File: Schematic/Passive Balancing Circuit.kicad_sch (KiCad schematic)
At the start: 70 parts, among them Q1 DMN2004K, Q2 DMN2004K, Q3 DMN2004K, Q4 DMN2004K, Q5 DMN2004K, Q6 DMN2004K, Q7 DMN2004K, Q8 DMN2004K

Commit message: 1st Schematic Review
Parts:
- renumbered C7 to C10, C8 to C11, C9 to C12, C10 to C13, C1 to C4, C2 to C5, C3 to C6, C4 to C7, C5 to C8, C6 to C9, R8 to R10, R9 to R11, R10 to R12, R11 to R13, R12 to R14, R13 to R15, R14 to R16, R15 to R17, R16 to R18, R17 to R19, R18 to R20, R19 to R21, R20 to R22, R21 to R23, R22 to R24, R23 to R25, R24 to R26, R25 to R27, R26 to R28, R27 to R29, R1 to R3, R28 to R30, R29 to R31, R30 to R32, R31 to R33, R32 to R34, R33 to R35, R34 to R36, R35 to R37, R2 to R4, R3 to R5, R4 to R6, R5 to R7, R6 to R8, R7 to R9

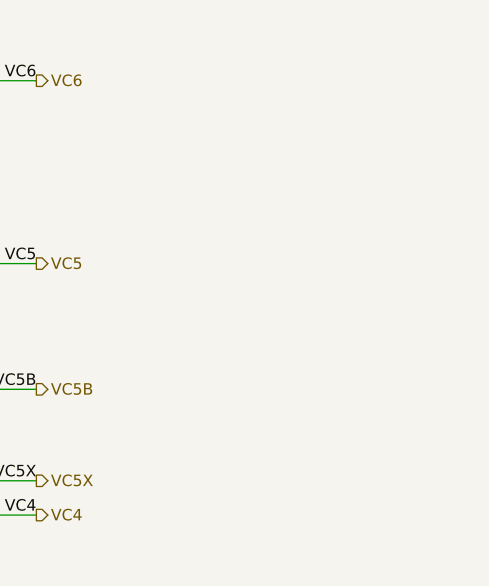
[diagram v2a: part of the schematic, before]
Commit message: added so many test points
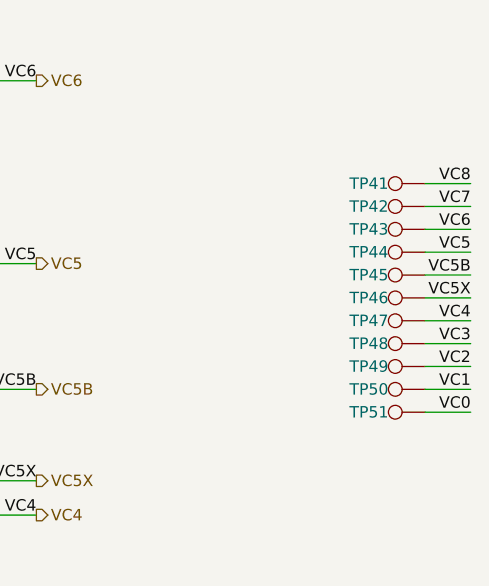
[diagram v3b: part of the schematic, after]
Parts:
- added TP41, TP42, TP43, TP44, TP45, TP46, TP47, TP48, TP49, TP50, TP51: TestPoint, symbol Connector:TestPoint
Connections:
- net VC0: now also TP51.1
- net VC1: now also TP50.1
- net VC2: now also TP49.1
- net VC3: now also TP48.1
- net VC4: now also TP47.1
- net VC5: now also TP44.1
- net VC5B: now also TP45.1
- net VC5X: now also TP46.1
- net VC6: now also TP43.1
- net VC7: now also TP42.1
- net VC8: now also TP41.1

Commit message: updates
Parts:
- renumbered TP41 to TP40, TP42 to TP41, TP43 to TP42, TP44 to TP43, TP45 to TP44, TP46 to TP45, TP47 to TP46, TP48 to TP47, TP49 to TP48, TP50 to TP49, TP51 to TP50
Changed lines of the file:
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@@
 		(on_board yes)
 		(dnp no)
-		(property "Reference" "TP41"
+		(property "Reference" "TP40"
 			(at 195.326 68.58 90)
 			(effects
@@
 			(project "STAR"
 				(path "/fc8533bc-25dd-4c20-9b4c-ffebebd6739b/e8da5d81-614b-4fe5-84b3-4c351fab7114/2e07670d-30e4-461b-a69e-227505cf7e3a"
-					(reference "TP41")
+					(reference "TP40")
 					(unit 1)
 				)
@@
 		(on_board yes)
 		(dnp no)
-		(property "Reference" "TP48"
+		(property "Reference" "TP47"
 			(at 195.326 86.36 90)
 			(effects
@@
 			(project "STAR"
 				(path "/fc8533bc-25dd-4c20-9b4c-ffebebd6739b/e8da5d81-614b-4fe5-84b3-4c351fab7114/2e07670d-30e4-461b-a69e-227505cf7e3a"
-					(reference "TP48")
+					(reference "TP47")
 					(unit 1)
 				)
@@
 		(on_board yes)
 		(dnp no)
-		(property "Reference" "TP49"
+		(property "Reference" "TP48"
 			(at 195.326 88.9 90)
 			(effects
@@
 			(project "STAR"
 				(path "/fc8533bc-25dd-4c20-9b4c-ffebebd6739b/e8da5d81-614b-4fe5-84b3-4c351fab7114/2e07670d-30e4-461b-a69e-227505cf7e3a"
-					(reference "TP49")
+					(reference "TP48")
 					(unit 1)
 				)
@@
 		(on_board yes)
 		(dnp no)
-		(property "Reference" "TP44"
+		(property "Reference" "TP43"
 			(at 195.326 76.2 90)
 			(effects
@@
 			(project "STAR"
 				(path "/fc8533bc-25dd-4c20-9b4c-ffebebd6739b/e8da5d81-614b-4fe5-84b3-4c351fab7114/2e07670d-30e4-461b-a69e-227505cf7e3a"
-					(reference "TP44")
+					(reference "TP43")
 					(unit 1)
 				)
@@
 		(on_board yes)
 		(dnp no)
-		(property "Reference" "TP47"
+		(property "Reference" "TP46"
 			(at 195.326 83.82 90)
 			(effects
@@
 			(project "STAR"
 				(path "/fc8533bc-25dd-4c20-9b4c-ffebebd6739b/e8da5d81-614b-4fe5-84b3-4c351fab7114/2e07670d-30e4-461b-a69e-227505cf7e3a"
-					(reference "TP47")
+					(reference "TP46")
 					(unit 1)
 				)
@@
 		(on_board yes)
 		(dnp no)
-		(property "Reference" "TP43"
+		(property "Reference" "TP42"
 			(at 195.326 73.66 90)
 			(effects
@@
 			(project "STAR"
 				(path "/fc8533bc-25dd-4c20-9b4c-ffebebd6739b/e8da5d81-614b-4fe5-84b3-4c351fab7114/2e07670d-30e4-461b-a69e-227505cf7e3a"
-					(reference "TP43")
+					(reference "TP42")
 					(unit 1)
 				)
@@
 		(on_board yes)
 		(dnp no)
-		(property "Reference" "TP45"
+		(property "Reference" "TP44"
 			(at 195.326 78.74 90)
 			(effects
@@
 			(project "STAR"
 				(path "/fc8533bc-25dd-4c20-9b4c-ffebebd6739b/e8da5d81-614b-4fe5-84b3-4c351fab7114/2e07670d-30e4-461b-a69e-227505cf7e3a"
-					(reference "TP45")
+					(reference "TP44")
 					(unit 1)
 				)
@@
 		(on_board yes)
 		(dnp no)
-		(property "Reference" "TP46"
+		(property "Reference" "TP45"
 			(at 195.326 81.28 90)
 			(effects
@@
 			(project "STAR"
 				(path "/fc8533bc-25dd-4c20-9b4c-ffebebd6739b/e8da5d81-614b-4fe5-84b3-4c351fab7114/2e07670d-30e4-461b-a69e-227505cf7e3a"
-					(reference "TP46")
+					(reference "TP45")
 					(unit 1)
 				)
@@
 		(on_board yes)
 		(dnp no)
-		(property "Reference" "TP51"
+		(property "Reference" "TP50"
 			(at 195.326 93.98 90)
 			(effects
@@
 			(project "STAR"
 				(path "/fc8533bc-25dd-4c20-9b4c-ffebebd6739b/e8da5d81-614b-4fe5-84b3-4c351fab7114/2e07670d-30e4-461b-a69e-227505cf7e3a"
-					(reference "TP51")
+					(reference "TP50")
 					(unit 1)
 				)
@@
 		(on_board yes)
 		(dnp no)
-		(property "Reference" "TP50"
+		(property "Reference" "TP49"
 			(at 195.326 91.44 90)
 			(effects
@@
 			(project "STAR"
 				(path "/fc8533bc-25dd-4c20-9b4c-ffebebd6739b/e8da5d81-614b-4fe5-84b3-4c351fab7114/2e07670d-30e4-461b-a69e-227505cf7e3a"
-					(reference "TP50")
+					(reference "TP49")
 					(unit 1)
 				)
@@
 		(on_board yes)
 		(dnp no)
-		(property "Reference" "TP42"
+		(property "Reference" "TP41"
 			(at 195.326 71.12 90)
 			(effects
@@
 			(project "STAR"
 				(path "/fc8533bc-25dd-4c20-9b4c-ffebebd6739b/e8da5d81-614b-4fe5-84b3-4c351fab7114/2e07670d-30e4-461b-a69e-227505cf7e3a"
-					(reference "TP42")
+					(reference "TP41")
 					(unit 1)
 				)

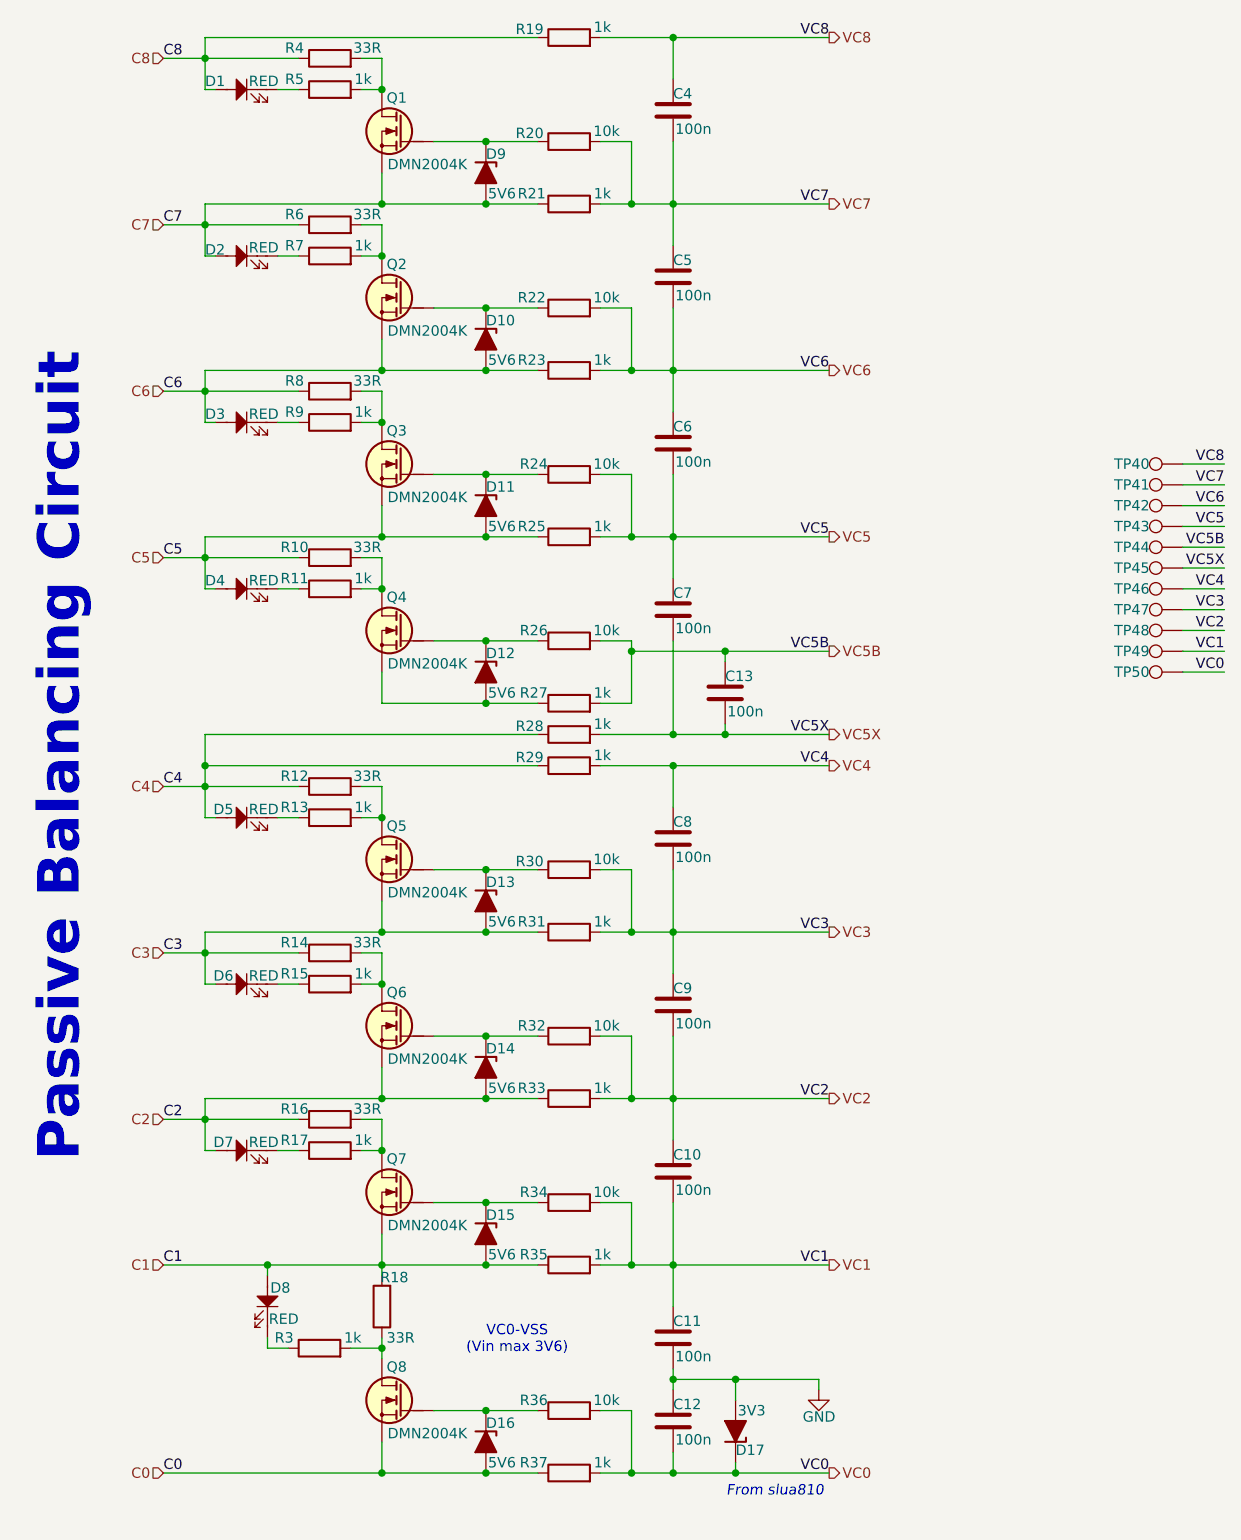
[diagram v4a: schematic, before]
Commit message: Added MCU
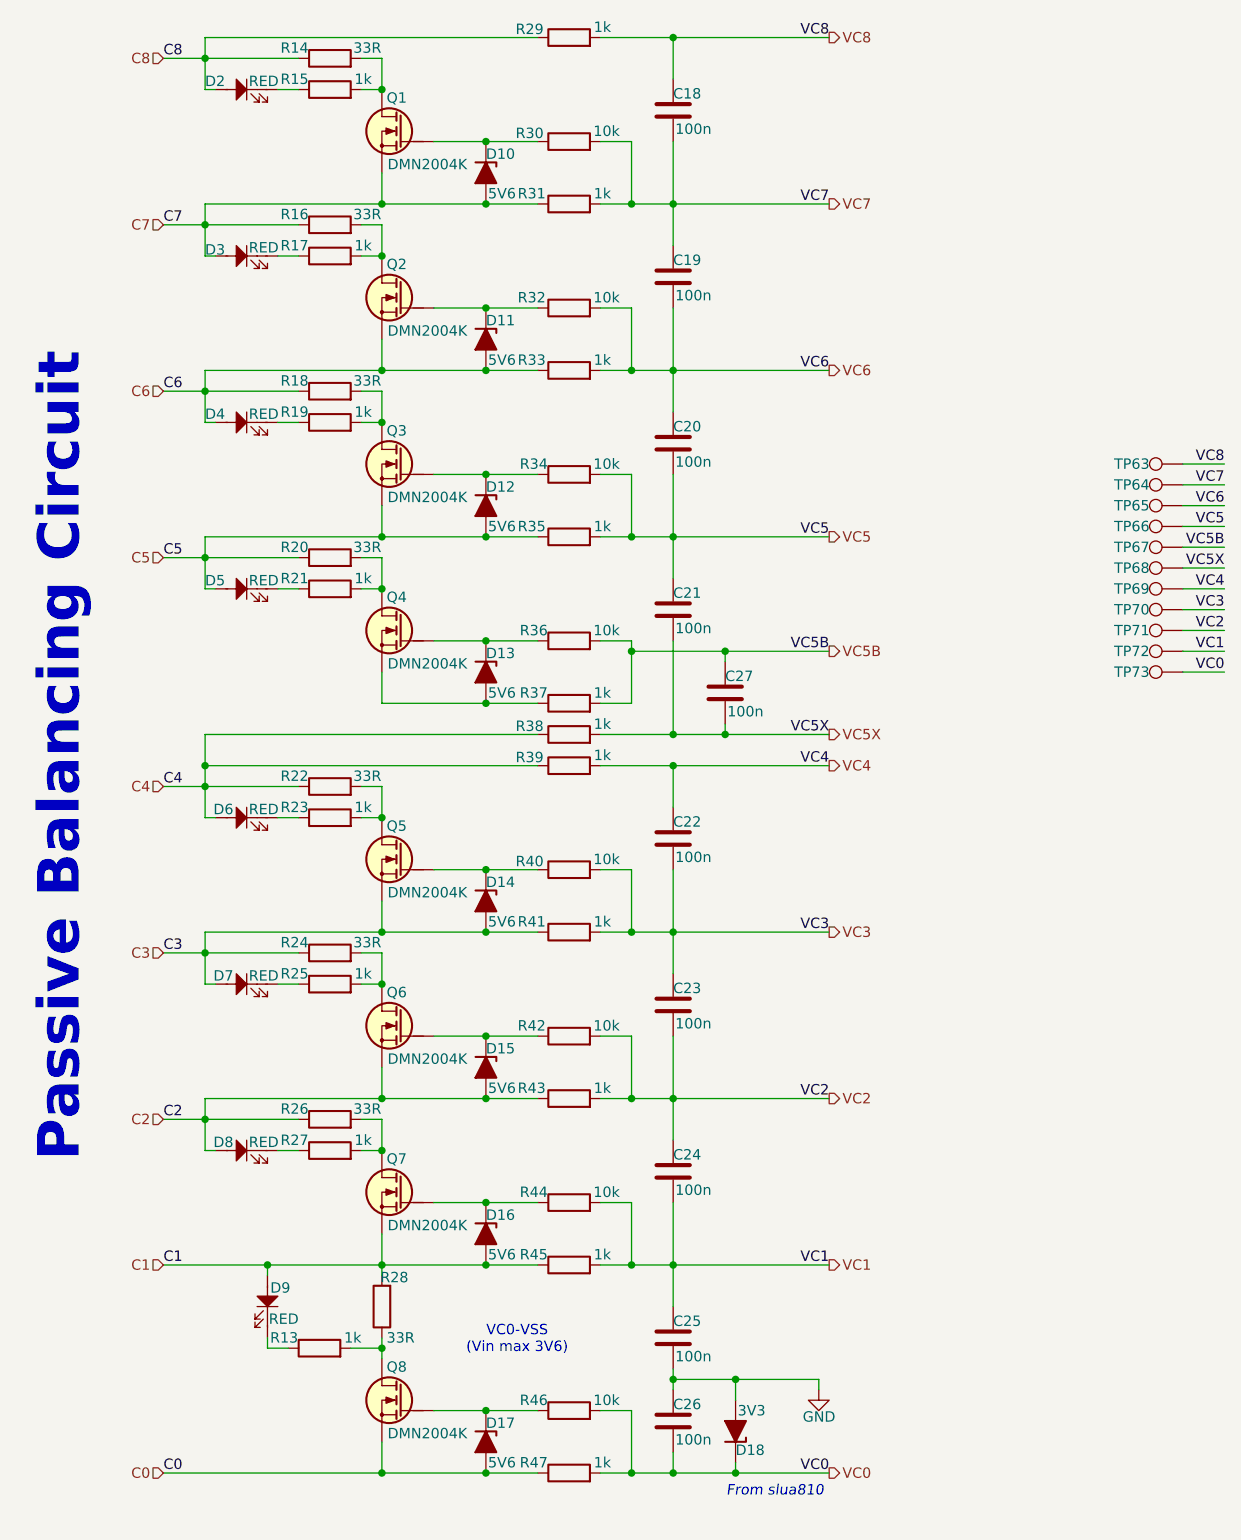
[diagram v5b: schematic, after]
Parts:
- renumbered C4 to C18, C5 to C19, C6 to C20, C7 to C21, C8 to C22, C9 to C23, C10 to C24, C11 to C25, C12 to C26, C13 to C27, D9 to D10, D10 to D11, D11 to D12, D12 to D13, D13 to D14, D14 to D15, D15 to D16, D16 to D17, D17 to D18, D1 to D2, D2 to D3, D3 to D4, D4 to D5, D5 to D6, D6 to D7, D7 to D8, D8 to D9, R3 to R13, R4 to R14, R5 to R15, R6 to R16, R7 to R17, R8 to R18, R9 to R19, R10 to R20, R11 to R21, R12 to R22, R13 to R23, R14 to R24, R15 to R25, R16 to R26, R17 to R27, R18 to R28, R19 to R29, R20 to R30, R21 to R31, R22 to R32, R23 to R33, R24 to R34, R25 to R35, R26 to R36, R27 to R37, R28 to R38, R29 to R39, R30 to R40, R31 to R41, R32 to R42, R33 to R43, R34 to R44, R35 to R45, R36 to R46, R37 to R47, TP40 to TP63, TP41 to TP64, TP42 to TP65, TP43 to TP66, TP44 to TP67, TP45 to TP68, TP46 to TP69, TP47 to TP70, TP48 to TP71, TP49 to TP72, TP50 to TP73

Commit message: Started to work on the BOM
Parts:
- removed C23, C24, C25, C26, C27: 100n, symbol Device:C
- removed D18: 3V3, symbol Device:D_Zener_Filled
- added C13, C14, C15, C16, C17: 220n, Capacitor_SMD:C_0805_2012Metric_Pad1.18x1.45mm_HandSolder, symbol Device:C
- C18, C19, C20, C21, C22: value 100n -> 220n; footprint (none) -> Capacitor_SMD:C_0805_2012Metric_Pad1.18x1.45mm_HandSolder; Link (none) -> https://mou.sr/42gipOV; Manufacturer Part Number (none) -> CL21B224KBFNFNE; Price per Unit (none) -> 0.10; Supplier (none) -> Mouser; Supplier Part Number (none) -> 187-CL21B224KBFNFNE
- D10, D11, D12, D13, D14, D15, D16, D17: footprint (none) -> DDZ5V6ASF-7:SODFL2512X75N; Link (none) -> https://mou.sr/47na3bQ; Manufacturer Part Number (none) -> DDZ9690-7; Price per Unit (none) -> 0.10; Supplier (none) -> Mouser; Supplier Part Number (none) -> 621-DDZ9690-7
- D2, D3, D4, D5, D6, D7, D8, D9: footprint PCM_Diode_SMD_AKL:D_0805_2012Metric -> ASMM-CR03-BU802:LEDM3528X210N; Link (none) -> https://mou.sr/460BFB7; Manufacturer Part Number (none) -> ASMM-CR03-BU802; Price per Unit (none) -> 0.32; Supplier (none) -> Mouser; Supplier Part Number (none) -> 630-ASMM-CR03-BU802
- Q1, Q2, Q3, Q4, Q5, Q6, Q7, Q8: footprint PCM_Package_TO_SOT_SMD_AKL:SOT-23 -> (none)
- renumbered R14 to R10, R15 to R11, R16 to R12, R17 to R13, R18 to R14, R19 to R15, R20 to R16, R21 to R17, R22 to R18, R23 to R19, R24 to R20, R25 to R21, R26 to R22, R27 to R23, R28 to R24, R29 to R25, R30 to R26, R31 to R27, R32 to R28, R33 to R29, R34 to R30, R35 to R31, R36 to R32, R37 to R33, R38 to R34, R39 to R35, R40 to R36, R41 to R37, R42 to R38, R43 to R39, R44 to R40, R45 to R41, R46 to R42, R47 to R43, R13 to R9, TP63 to TP40, TP64 to TP41, TP65 to TP42, TP66 to TP43, TP67 to TP44, TP68 to TP45, TP69 to TP46, TP70 to TP47, TP71 to TP48, TP72 to TP49, TP73 to TP50
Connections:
- net GND: now also C21.2
- net VC0: now also C20.2, C21.1
- net VC1: now also C19.2, C20.1
- net VC2: now also C18.2, C19.1
- net VC3: now also C18.1, C17.2; no longer C22.2
- net VC4: now also C17.1; no longer C22.1
- net VC5: now also C15.2, C16.1; no longer C20.2, C21.1
- net VC5B: now also C22.1
- net VC5X: now also C22.2, C16.2; no longer C21.2
- net VC6: now also C14.2, C15.1; no longer C19.2, C20.1
- net VC7: now also C13.2, C14.1; no longer C18.2, C19.1
- net VC8: now also C13.1; no longer C18.1

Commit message: Massive pivit, simplification
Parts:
- renumbered C17 to C10, C18 to C11, C19 to C12, C20 to C13, C21 to C14, C22 to C15, C13 to C6, C14 to C7, C15 to C8, C16 to C9, D2 to D1, D11 to D10, D12 to D11, D13 to D12, D14 to D13, D15 to D14, D16 to D15, D17 to D16, D3 to D2, D4 to D3, D5 to D4, D6 to D5, D7 to D6, D8 to D7, D9 to D8, D10 to D9, TP40 to TP33, TP41 to TP34, TP42 to TP35, TP43 to TP36, TP44 to TP37, TP45 to TP38, TP46 to TP39, TP47 to TP40, TP48 to TP41, TP49 to TP42, TP50 to TP43
